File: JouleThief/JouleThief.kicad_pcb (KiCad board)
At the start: 2 copper layers, 8 parts, among them J1 Screw_Terminal_01x02, J2 Screw_Terminal_01x02, Q1 BC547, Q2 BC547

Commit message: Finished PCB
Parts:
- added D1: LED, LED_THT:LED_D5.0mm_Clear, F.Cu at (151.4, 95.2)
- added R3: 300, Resistor_THT:R_Axial_DIN0204_L3.6mm_D1.6mm_P7.62mm_Horizontal, F.Cu at (144.8, 94.5)
- added S1: SWITCH-SPDT-PTH-11.6X4.0MM-KIT, SnapEDA Library:SW_1825159-1, F.Cu at (152.9, 101.9)
- moved L1 32.3 mm to (162.1, 93.7), turned to -90 degrees
- moved J1 25.8 mm to (169.3, 101.1), turned to 90 degrees
- moved Q2 15.9 mm to (139.4, 96.4)
- moved R2 14.0 mm to (128.3, 94.7)
- moved R1 13.7 mm to (128.3, 98.6)
- moved Q1 12.9 mm to (139.4, 102.9)
- moved J2 9.50 mm to (122.4, 96.0), turned to -90 degrees
- moved C1 3.06 mm to (128.3, 103.1)
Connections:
- J1 pad 2: Net-(C1-Pad1) -> Net-(J1-Pad2)
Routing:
- net Net-(J2-Pad1): track 0.00 -> 47.9 mm
- net Net-(C1-Pad1): track 0.00 -> 45.0 mm
- net Net-(J1-Pad2): track 0.00 -> 16.3 mm
- net Net-(Q1-Pad2): track 0.00 -> 11.0 mm
- net Net-(C1-Pad2): track 0.00 -> 10.7 mm
- net Net-(D1-Pad2): track 0.00 -> 7.90 mm
- net Net-(D1-Pad1): track 0.00 -> 6.85 mm
- added copper zone on B.Cu, net GND
- added copper zone on F.Cu, net GND
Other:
- board outline added: 55.3 x 13.2 mm

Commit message: silkscreen enh
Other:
- board text added: "+"
- board text added: "-"
- board text added: "1.5V Typical"
- board text added: "D1"
- board text added: "Designed by: Casper R. Tak"
- board text added: "Input"
- board text added: "J1"
- board text added: "JouleThief V1.0"
- board text added: "Output"
- board text added: "←•→"
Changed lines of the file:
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@@
     )
   )
+  (gr_line (start 147.955 104.521) (end 147.955 102.743) (layer "B.SilkS") (width 0.15))
+  (gr_line (start 157.607 102.743) (end 157.607 104.521) (layer "B.SilkS") (width 0.15))
+  (gr_line (start 147.955 102.743) (end 157.607 102.743) (layer "B.SilkS") (width 0.15))
+  (gr_line (start 157.607 104.521) (end 147.955 104.521) (layer "B.SilkS") (width 0.15))
   (gr_arc (start 173.624915 103.124) (mid 173.029756 104.560841) (end 171.592915 105.156) (layer "Edge.Cuts") (width 0.1))
   (gr_arc (start 171.592915 91.948) (mid 173.029756 92.543159) (end 173.624915 93.98) (layer "Edge.Cuts") (width 0.1))
@@
   (gr_arc (start 120.396 105.156) (mid 118.959159 104.560841) (end 118.364 103.124) (layer "Edge.Cuts") (width 0.1))
   (gr_line (start 171.592915 105.156) (end 120.396 105.156) (layer "Edge.Cuts") (width 0.1))
+  (gr_text "Designed by:\nCasper R. Tak" (at 154.051 98.425) (layer "B.SilkS")
+    (effects (font (size 1.5 1.5) (thickness 0.3)) (justify mirror))
+  )
+  (gr_text "J1" (at 156.464 103.6828) (layer "B.SilkS")
+    (effects (font (size 1 1) (thickness 0.25)) (justify mirror))
+  )
+  (gr_text "D1\n" (at 149.098 103.6828) (layer "B.SilkS")
+    (effects (font (size 1 1) (thickness 0.25)) (justify mirror))
+  )
+  (gr_text "Output\n" (at 168.656 93.091) (layer "B.SilkS")
+    (effects (font (size 1.5 1.5) (thickness 0.3)) (justify mirror))
+  )
+  (gr_text "-\n" (at 171.958 101.092) (layer "B.SilkS")
+    (effects (font (size 1 1) (thickness 0.25)) (justify mirror))
+  )
+  (gr_text "+" (at 171.958 95.885) (layer "B.SilkS")
+    (effects (font (size 1 1) (thickness 0.25)) (justify mirror))
+  )
+  (gr_text " ←•→" (at 153.416 103.5558) (layer "B.SilkS")
+    (effects (font (size 1.3 1.3) (thickness 0.25)) (justify mirror))
+  )
+  (gr_text "1.5V Typical" (at 122.936 103.505) (layer "B.SilkS")
+    (effects (font (size 0.9 0.9) (thickness 0.15)) (justify mirror))
+  )
+  (gr_text "Input" (at 123.952 93.091) (layer "B.SilkS")
+    (effects (font (size 1.5 1.5) (thickness 0.3)) (justify mirror))
+  )
+  (gr_text "JouleThief V1.0\n" (at 135.382 100.711) (layer "B.SilkS")
+    (effects (font (size 1.5 1.5) (thickness 0.3)) (justify mirror))
+  )
+  (gr_text "+" (at 119.761 95.885) (layer "B.SilkS")
+    (effects (font (size 1 1) (thickness 0.25)) (justify mirror))
+  )
+  (gr_text "-\n" (at 119.888 100.965) (layer "B.SilkS")
+    (effects (font (size 1 1) (thickness 0.25)) (justify mirror))
+  )
   (segment (start 130.93163 104.648) (end 136.533334 104.648) (width 0.5) (layer "F.Cu") (net 1))
   (segment (start 128.3 98.6328) (end 128.27 98.6028) (width 0.5) (layer "F.Cu") (net 1))

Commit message: enh silkscreen
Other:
- board text added: "A"
- board text added: "C"
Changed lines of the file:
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@@
     (effects (font (size 1 1) (thickness 0.25)) (justify mirror))
+  )
+  (gr_text "A" (at 153.924 93.5228) (layer "F.SilkS")
+    (effects (font (size 1 1) (thickness 0.25)))
+  )
+  (gr_text "C" (at 151.4856 93.5736) (layer "F.SilkS")
+    (effects (font (size 1 1) (thickness 0.25)))
   )
   (segment (start 130.93163 104.648) (end 136.533334 104.648) (width 0.5) (layer "F.Cu") (net 1))

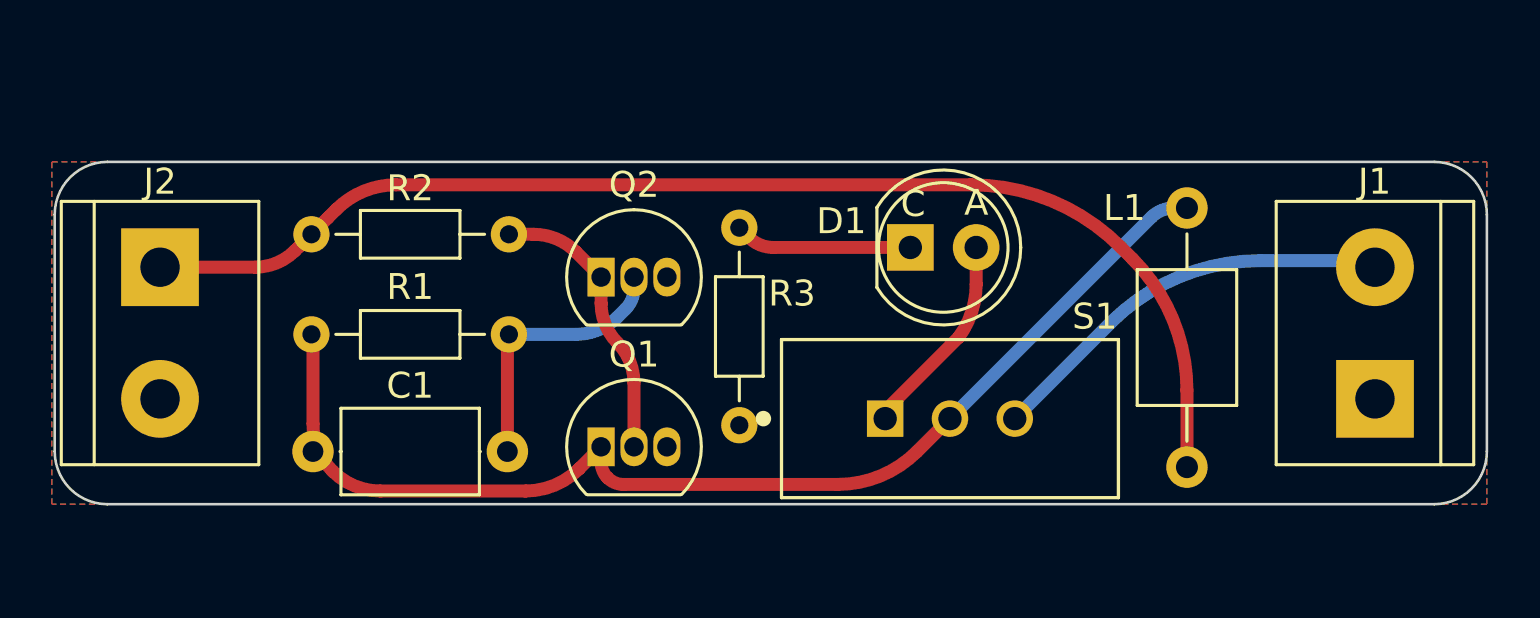
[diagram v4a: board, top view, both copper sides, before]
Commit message: Finished SMD JouleThief functional
added silkscreen
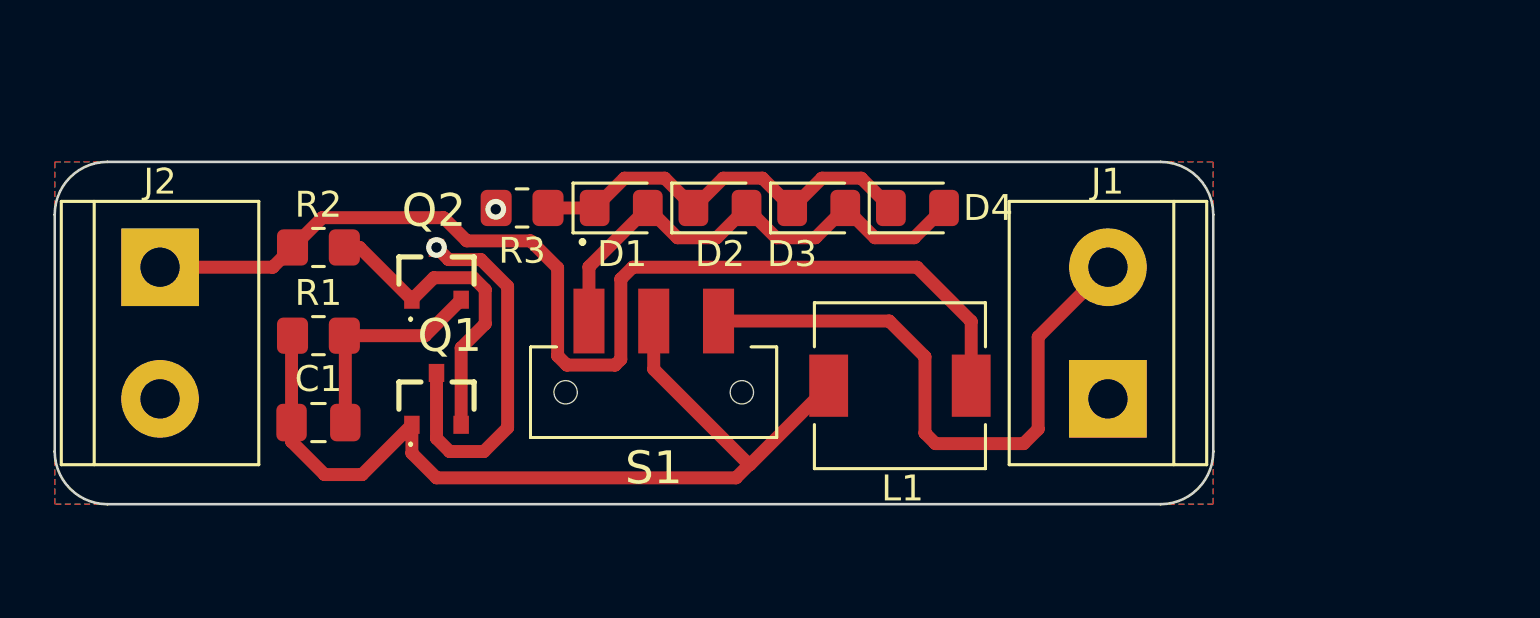
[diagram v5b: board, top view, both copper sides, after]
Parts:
- added D2: LED, LED_SMD:LED_0805_2012Metric_Pad1.15x1.40mm_HandSolder, F.Cu at (144.0, 93.7)
- added D3: LED, LED_SMD:LED_0805_2012Metric_Pad1.15x1.40mm_HandSolder, F.Cu at (147.8, 93.7)
- added D4: LED, LED_SMD:LED_0805_2012Metric_Pad1.15x1.40mm_HandSolder, F.Cu at (151.7, 93.7)
- C1: footprint Capacitor_THT:C_Axial_L5.1mm_D3.1mm_P7.50mm_Horizontal -> Capacitor_SMD:C_0805_2012Metric_Pad1.18x1.45mm_HandSolder
- D1: footprint LED_THT:LED_D5.0mm_Clear -> LED_SMD:LED_0805_2012Metric_Pad1.15x1.40mm_HandSolder
- L1: footprint Inductor_THT:L_Axial_L5.0mm_D3.6mm_P10.00mm_Horizontal_Murata_BL01RN1A2A2 -> Inductor_SMD:L_6.3x6.3_H3
- Q1, Q2: footprint Package_TO_SOT_THT:TO-92_Inline -> SamacSys_Parts:BC847215
- R1, R2: footprint Resistor_THT:R_Axial_DIN0204_L3.6mm_D1.6mm_P7.62mm_Horizontal -> Resistor_SMD:R_0805_2012Metric_Pad1.20x1.40mm_HandSolder
- R3: value 300 -> x; footprint Resistor_THT:R_Axial_DIN0204_L3.6mm_D1.6mm_P7.62mm_Horizontal -> Resistor_SMD:R_0805_2012Metric_Pad1.20x1.40mm_HandSolder
- S1: footprint SnapEDA Library:SW_1825159-1 -> SamacSys_Parts:LSSM12PVTR
- moved L1 13.0 mm to (151.0, 100.6), turned to 0 degrees
- moved S1 11.5 mm to (141.5, 100.8)
- moved D1 11.3 mm to (140.2, 93.7)
- moved J1 10.3 mm to (159.0, 101.1)
- moved R3 8.42 mm to (136.4, 93.7), turned to 180 degrees
- moved Q1 6.61 mm to (133.1, 101.1)
- moved Q2 6.35 mm to (133.1, 96.3)
- moved C1 1.14 mm to (128.5, 102.0)
- moved R2 0.58 mm to (128.5, 95.2)
- moved R1 0.27 mm to (128.5, 98.7)
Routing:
- net GND: track 0.00 -> 14.7 mm, vias 0 -> 2
- net Net-(D4-Pad2): track 7.90 -> 19.6 mm
- net Net-(D4-Pad1): track 6.85 -> 16.1 mm
- net Net-(C1-Pad1): track 45.0 -> 36.4 mm
- net Net-(J1-Pad2): track 16.3 -> 23.6 mm
- net Net-(J2-Pad1): track 47.9 -> 43.2 mm
- net Net-(C1-Pad2): track 10.7 -> 8.45 mm
- net Net-(Q1-Pad2): track 11.0 -> 12.4 mm
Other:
- board size 55.3 x 13.2 mm -> 44.7 x 13.2 mm
- board text removed: "A"
- board text removed: "C"

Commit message: production and smooth traces add
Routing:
- net Net-(J2-Pad1): track 43.2 -> 42.3 mm
- net Net-(D4-Pad2): track 19.6 -> 18.9 mm
- net Net-(D4-Pad1): track 16.1 -> 15.6 mm
- net Net-(J1-Pad2): track 23.6 -> 23.1 mm
